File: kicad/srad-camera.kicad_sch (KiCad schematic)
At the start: 14 parts, among them J1 DEBUG, SW1 POWER, SW2 USER, SW3 BOOT0

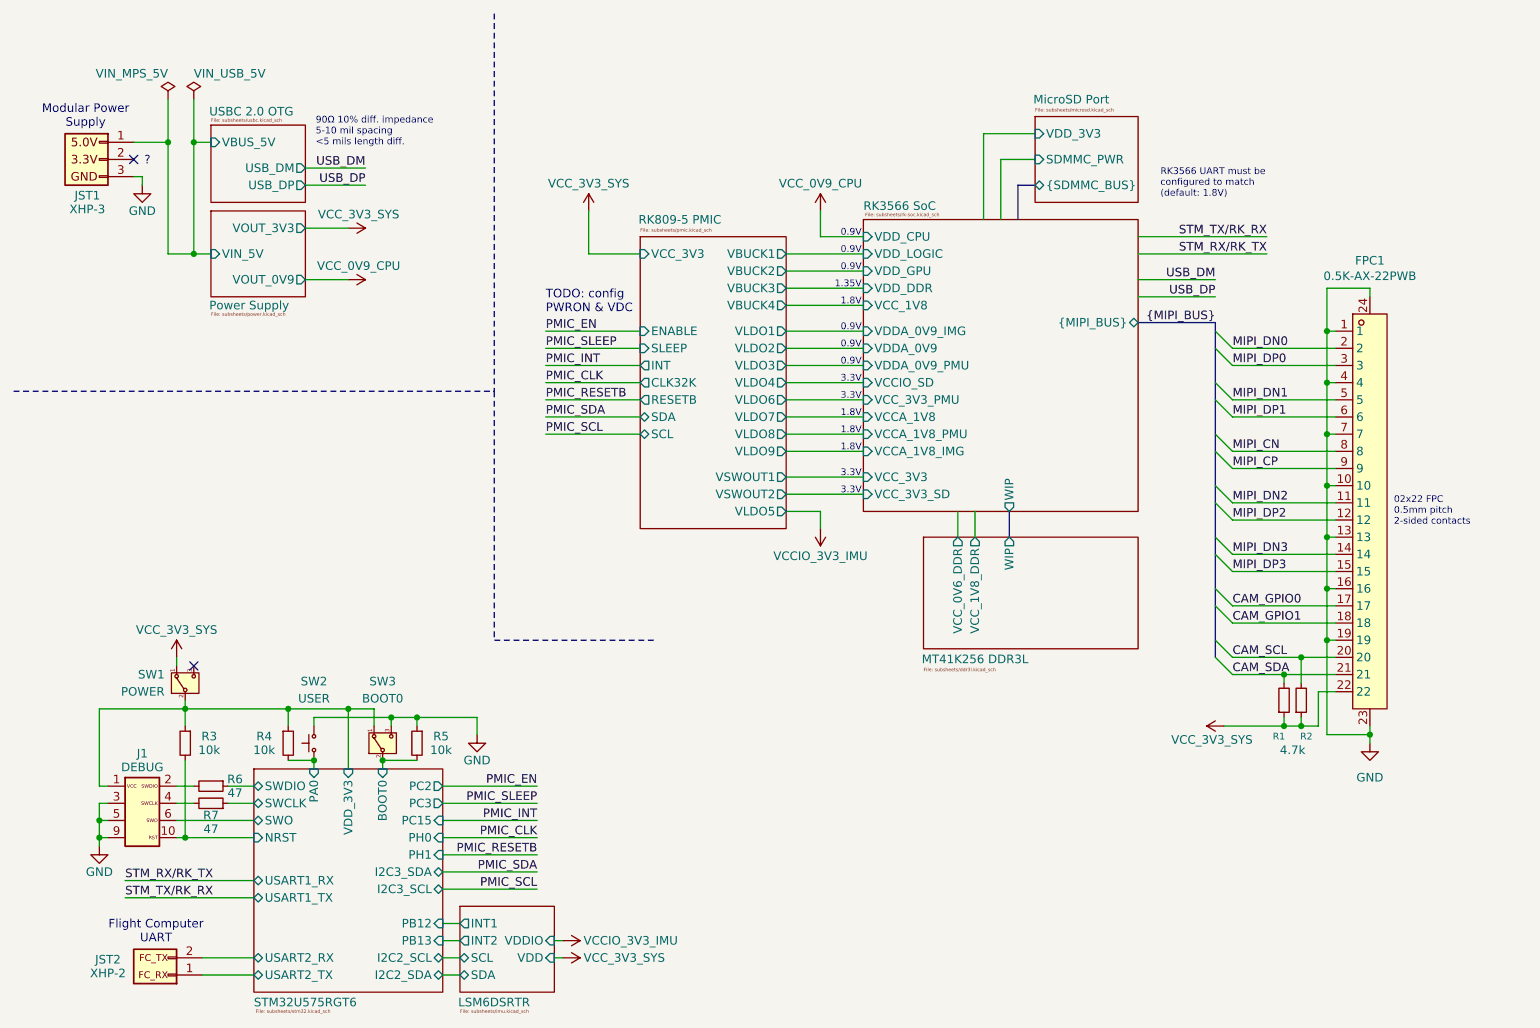
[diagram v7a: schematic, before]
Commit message: Finalized PMIC and added control from STM32
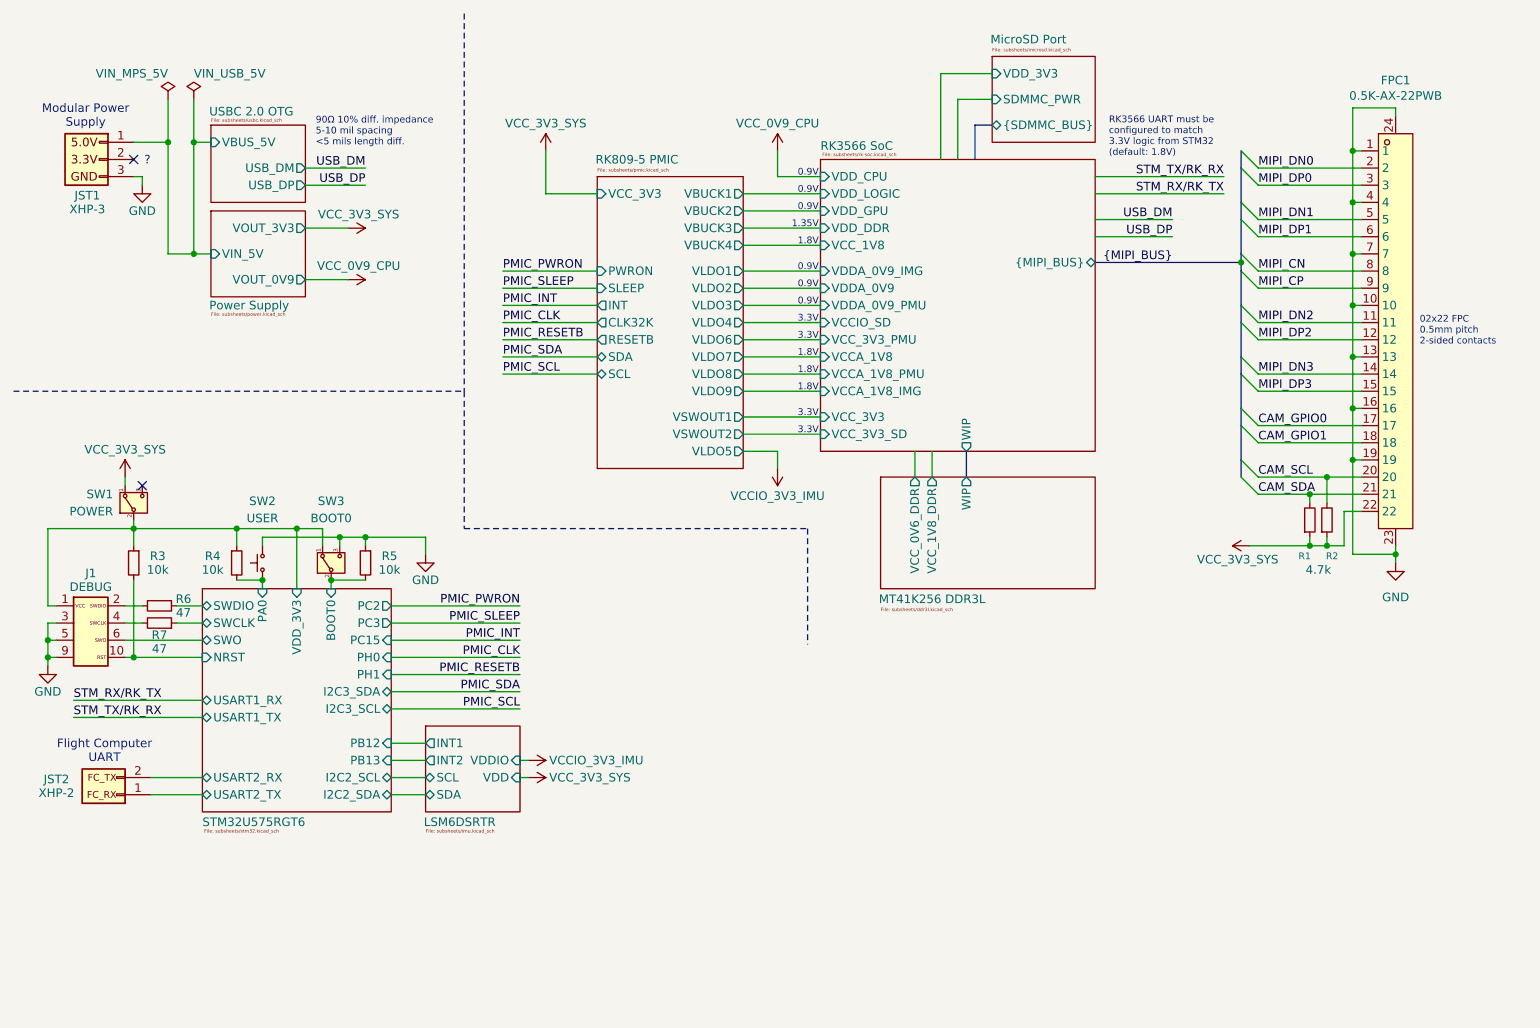
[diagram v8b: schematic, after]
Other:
- sheet RK809-5 PMIC ports: added PWRON; removed ENABLE
- note added: "RK3566 UART must be configured to match 3.3V logic from STM32 (default: 1.8V)"
- note removed: "RK3566 UART must be configured to match (default: 1.8V)"
- note removed: "TODO: config PWRON & VDC"
- moved on the sheet: FPC1, J1, JST2, R1, R2, R3, R4, R5, R6, R7, SW1, SW2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
